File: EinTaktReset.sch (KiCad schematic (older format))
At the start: 64 parts

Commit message: bus improved
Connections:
- net labels added: a0, a1, a2, a3, a4, a5, a6, a7
- wire segments 112 -> 120
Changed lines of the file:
@@
 Wire Wire Line
 	4050 1250 4050 1100
-Wire Bus Line
-	3000 1000 3950 1000
-Wire Bus Line
-	3000 1000 3000 850
-Wire Bus Line
-	3000 850  3600 850
 Wire Wire Line
 	1450 6400 1150 6400
@@
 	4000 12750 4200 12750
 Wire Wire Line
-	5400 12000 4750 12000
-Wire Wire Line
-	4750 12000 4750 11000
+	4750 12000 5400 12000
+Wire Wire Line
+	4750 11000 4750 12000
 Wire Wire Line
 	4750 11000 5400 11000
@@
 	6950 10850 6950 13200
 Wire Wire Line
-	7750 13200 7750 10850
+	7750 10850 7750 13200
 Connection ~ 6950 11500
 Connection ~ 7750 12000
+Text Label 3350 1200 1    60   ~ 0
+a0
+Text Label 3450 1200 1    60   ~ 0
+a1
+Text Label 3550 1200 1    60   ~ 0
+a2
+Text Label 3650 1200 1    60   ~ 0
+a3
+Text Label 3750 1200 1    60   ~ 0
+a4
+Text Label 3850 1200 1    60   ~ 0
+a5
+Text Label 3950 1200 1    60   ~ 0
+a6
+Text Label 4050 1200 1    60   ~ 0
+a7
+Wire Wire Line
+	1950 750  2100 750
+Wire Wire Line
+	1950 850  2100 850
+Wire Wire Line
+	1950 950  2100 950
+Wire Wire Line
+	1950 1050 2100 1050
+Wire Wire Line
+	1950 1150 2100 1150
+Wire Wire Line
+	1950 1250 2100 1250
+Wire Wire Line
+	1950 1350 2100 1350
+Wire Wire Line
+	1950 1450 2100 1450
+Entry Wire Line
+	2100 750  2200 850
+Entry Wire Line
+	2100 850  2200 950
+Entry Wire Line
+	2100 950  2200 1050
+Entry Wire Line
+	2100 1050 2200 1150
+Entry Wire Line
+	2100 1150 2200 1250
+Entry Wire Line
+	2100 1250 2200 1350
+Entry Wire Line
+	2100 1350 2200 1450
+Entry Wire Line
+	2100 1450 2200 1550
+Wire Bus Line
+	3950 1000 2200 1000
+Wire Bus Line
+	2200 850  2200 1550
+Text Label 2050 750  2    60   ~ 0
+a0
+Text Label 2050 850  2    60   ~ 0
+a1
+Text Label 2050 950  2    60   ~ 0
+a2
+Text Label 2050 1050 2    60   ~ 0
+a3
+Text Label 2050 1150 2    60   ~ 0
+a4
+Text Label 2050 1250 2    60   ~ 0
+a5
+Text Label 2050 1350 2    60   ~ 0
+a6
+Text Label 2050 1450 2    60   ~ 0
+a7
 $EndSCHEMATC

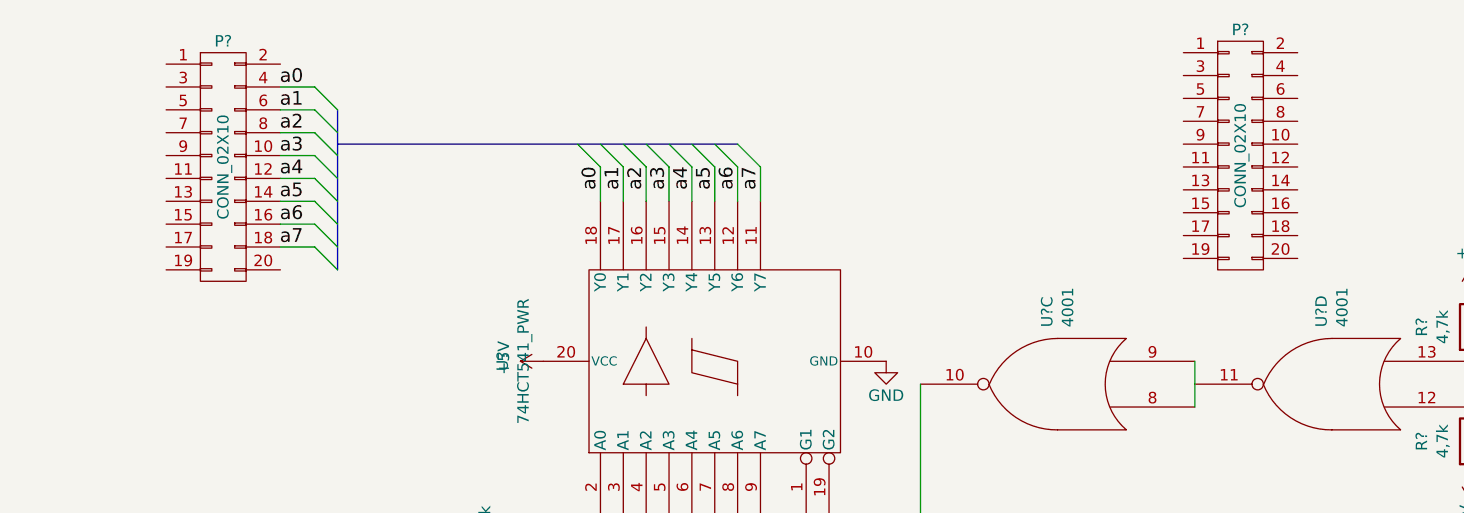
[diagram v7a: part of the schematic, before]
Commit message: busverbindungen in eintaktreset fertig gezeichnet
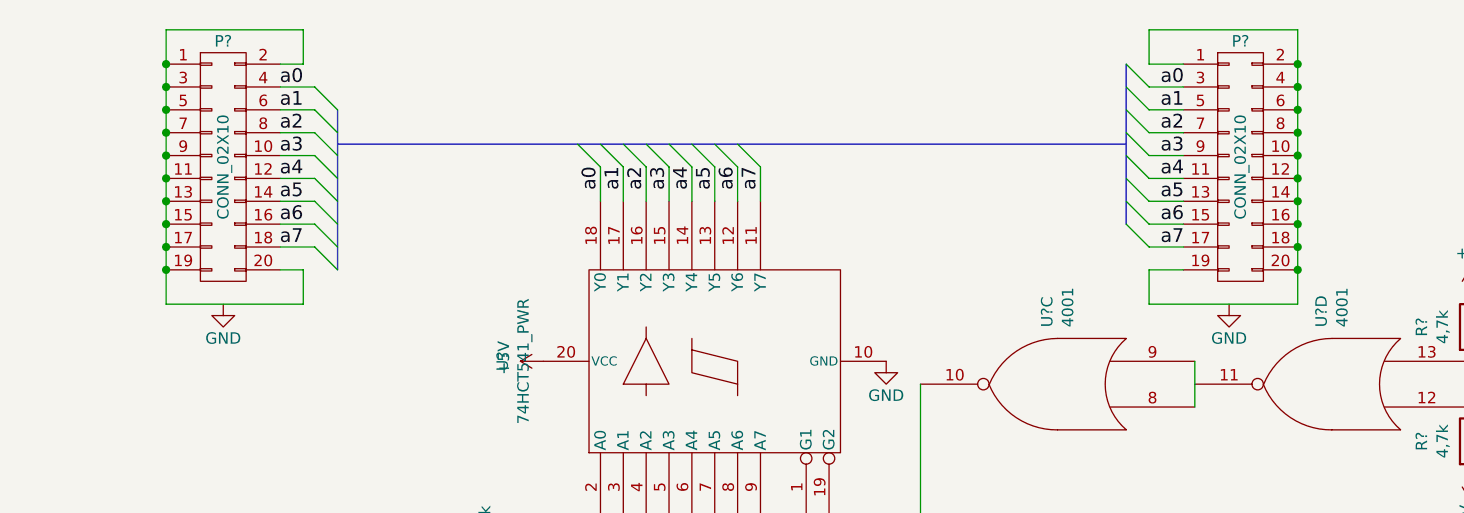
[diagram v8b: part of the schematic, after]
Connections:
- wire segments 120 -> 142
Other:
- moved on the sheet: P?
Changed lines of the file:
@@
 L CONN_02X10 P?
 U 1 1 5A28337D
-P 6150 1050
-F 0 "P?" H 6150 1600 50  0000 C CNN
-F 1 "CONN_02X10" V 6150 1050 50  0000 C CNN
-F 2 "" H 6150 -150 50  0000 C CNN
-F 3 "" H 6150 -150 50  0000 C CNN
-	1    6150 1050
+P 6150 1100
+F 0 "P?" H 6150 1650 50  0000 C CNN
+F 1 "CONN_02X10" V 6150 1100 50  0000 C CNN
+F 2 "" H 6150 -100 50  0000 C CNN
+F 3 "" H 6150 -100 50  0000 C CNN
+	1    6150 1100
 	1    0    0    -1
 $EndComp
@@
 	2100 1450 2200 1550
 Wire Bus Line
-	3950 1000 2200 1000
+	2200 1000 5650 1000
 Wire Bus Line
 	2200 850  2200 1550
@@
 Text Label 2050 1450 2    60   ~ 0
 a7
+Wire Wire Line
+	1950 650  2050 650
+Wire Wire Line
+	2050 650  2050 500
+Wire Wire Line
+	2050 500  1450 500
+Wire Wire Line
+	1450 500  1450 1700
+Connection ~ 1450 650
+Connection ~ 1450 750
+Connection ~ 1450 850
+Connection ~ 1450 950
+Connection ~ 1450 1050
+Connection ~ 1450 1150
+Connection ~ 1450 1250
+Connection ~ 1450 1350
+Connection ~ 1450 1450
+Wire Wire Line
+	1950 1550 2050 1550
+Wire Wire Line
+	2050 1550 2050 1700
+Wire Wire Line
+	2050 1700 1450 1700
+Connection ~ 1450 1550
+$Comp
+L GND #PWR?
+U 1 1 5A384C6C
+P 1700 1700
+F 0 "#PWR?" H 1700 1450 50  0001 C CNN
+F 1 "GND" H 1700 1550 50  0000 C CNN
+F 2 "" H 1700 1700 50  0001 C CNN
+F 3 "" H 1700 1700 50  0001 C CNN
+	1    1700 1700
+	1    0    0    -1
+$EndComp
+Wire Wire Line
+	5900 650  5750 650
+Wire Wire Line
+	5900 750  5750 750
+Wire Wire Line
+	5900 850  5750 850
+Wire Wire Line
+	5900 950  5750 950
+Wire Wire Line
+	5900 1050 5750 1050
+Wire Wire Line
+	5900 1150 5750 1150
+Wire Wire Line
+	5900 1250 5750 1250
+Wire Wire Line
+	5750 650  5750 500
+Wire Wire Line
+	5750 500  6400 500
+Wire Wire Line
+	6400 500  6400 1700
+Wire Wire Line
+	5900 1350 5750 1350
+Wire Wire Line
+	5900 1450 5750 1450
+Wire Wire Line
+	5900 1550 5750 1550
+Connection ~ 6400 650
+Connection ~ 6400 750
+Connection ~ 6400 850
+Connection ~ 6400 950
+Connection ~ 6400 1050
+Connection ~ 6400 1150
+Connection ~ 6400 1250
+Connection ~ 6400 1350
+Connection ~ 6400 1450
+Wire Wire Line
+	6400 1700 5750 1700
+Wire Wire Line
+	5750 1700 5750 1550
+Connection ~ 6400 1550
+Entry Wire Line
+	5650 650  5750 750
+Entry Wire Line
+	5650 750  5750 850
+Entry Wire Line
+	5650 850  5750 950
+Entry Wire Line
+	5650 950  5750 1050
+Entry Wire Line
+	5650 1050 5750 1150
+Entry Wire Line
+	5650 1150 5750 1250
+Entry Wire Line
+	5650 1250 5750 1350
+Entry Wire Line
+	5650 1350 5750 1450
+Wire Bus Line
+	5650 650  5650 1350
+Text Label 5800 750  0    60   ~ 0
+a0
+Text Label 5800 850  0    60   ~ 0
+a1
+Text Label 5800 950  0    60   ~ 0
+a2
+Text Label 5800 1050 0    60   ~ 0
+a3
+Text Label 5800 1150 0    60   ~ 0
+a4
+Text Label 5800 1250 0    60   ~ 0
+a5
+Text Label 5800 1350 0    60   ~ 0
+a6
+Text Label 5800 1450 0    60   ~ 0
+a7
+$Comp
+L GND #PWR?
+U 1 1 5A389DC9
+P 6100 1700
+F 0 "#PWR?" H 6100 1450 50  0001 C CNN
+F 1 "GND" H 6100 1550 50  0000 C CNN
+F 2 "" H 6100 1700 50  0001 C CNN
+F 3 "" H 6100 1700 50  0001 C CNN
+	1    6100 1700
+	1    0    0    -1
+$EndComp
 $EndSCHEMATC
